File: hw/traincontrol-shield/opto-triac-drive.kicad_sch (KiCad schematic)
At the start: 6 parts, among them U5 MOC3021M, U6 MOC3021M

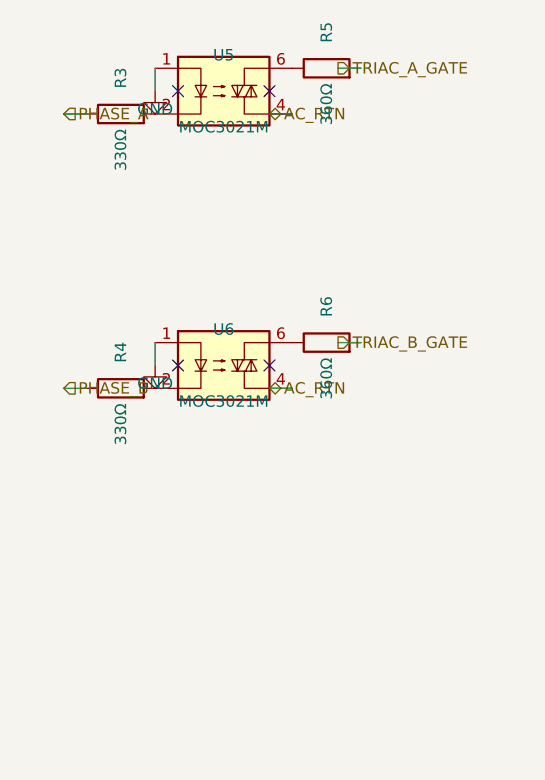
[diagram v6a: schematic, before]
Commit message: Disperse component layout and triple wire stub length across all sheets
- STUB: 2.54 → 7.62 mm (3×) in all three generator scripts
- Inter-component spacing doubled in power-supply, MCU, and logic sheets
- Top-level inter-column gap widened (LX 120 → 130 mm) to avoid label collision
- Sheet frame heights made variable per pin count (20–35 mm)
- Right-column sheet x-origin and connector J4/J5/J6 x-positions updated accordingly
- All 8 sheets regenerated and validated with kicad-cli

Co-Authored-By: Claude Sonnet 4.6 <noreply@anthropic.com>
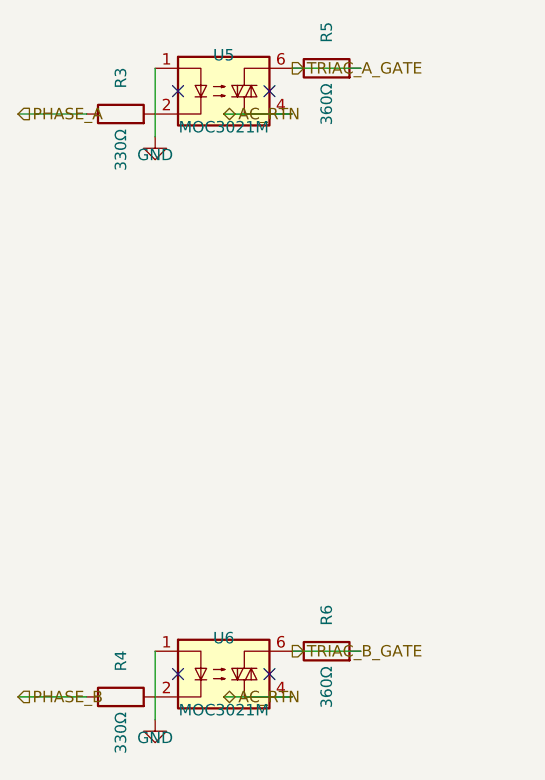
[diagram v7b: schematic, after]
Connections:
- net TRIAC_A_GATE: now also R5.1, U5.6
- net TRIAC_B_GATE: now also R6.1, U6.6
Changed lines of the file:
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@@
 	)
 	(wire
-		(pts (xy 72.39 87.63) (xy 72.39 90.17))
+		(pts (xy 72.39 87.63) (xy 72.39 95.25))
 		(stroke (width 0) (type solid))
 	)
 	(symbol
 		(lib_id "power:GND")
-		(at 72.39 90.17 0)
+		(at 72.39 95.25 0)
 		(unit 1)
 		(exclude_from_sim no)
@@
 		(dnp no)
 		(property "Reference" "#PWR03"
-			(at 72.39 88.17 0)
+			(at 72.39 93.25 0)
 			(effects (font (size 1.27 1.27)) (hide yes))
 		)
 		(property "Value" "GND"
-			(at 72.39 92.17 0)
+			(at 72.39 97.25 0)
 			(effects (font (size 1.27 1.27)))
 		)
 		(property "Footprint" ""
-			(at 72.39 90.17 0)
+			(at 72.39 95.25 0)
 			(effects (font (size 1.27 1.27)) (hide yes))
 		)
 		(property "Datasheet" ""
-			(at 72.39 90.17 0)
+			(at 72.39 95.25 0)
 			(effects (font (size 1.27 1.27)) (hide yes))
 		)
@@
 	)
 	(wire
-		(pts (xy 85.09 92.71000000000001) (xy 87.63000000000001 92.71000000000001))
+		(pts (xy 80.01 92.71000000000001) (xy 87.63000000000001 92.71000000000001))
 		(stroke (width 0) (type solid))
 	)
 	(hierarchical_label "AC_RTN"
 		(shape bidirectional)
-		(at 85.09 92.71000000000001 0)
-		(fields_autoplaced yes)
-		(effects (font (size 1.27 1.27)) (justify left bottom))
-		(property "Intersheetrefs" "${INTERSHEET_REFS}"
-			(at 85.09 92.71000000000001 0)
+		(at 80.01 92.71000000000001 0)
+		(fields_autoplaced yes)
+		(effects (font (size 1.27 1.27)) (justify left bottom))
+		(property "Intersheetrefs" "${INTERSHEET_REFS}"
+			(at 80.01 92.71000000000001 0)
 			(effects (font (size 1.27 1.27)) (hide yes))
 		)
@@
 	)
 	(wire
-		(pts (xy 62.23 92.71000000000001) (xy 64.77 92.71000000000001))
+		(pts (xy 57.15 92.71000000000001) (xy 64.77 92.71000000000001))
 		(stroke (width 0) (type solid))
 	)
 	(hierarchical_label "PHASE_A"
 		(shape input)
-		(at 62.23 92.71000000000001 0)
-		(fields_autoplaced yes)
-		(effects (font (size 1.27 1.27)) (justify left bottom))
-		(property "Intersheetrefs" "${INTERSHEET_REFS}"
-			(at 62.23 92.71000000000001 0)
+		(at 57.15 92.71000000000001 0)
+		(fields_autoplaced yes)
+		(effects (font (size 1.27 1.27)) (justify left bottom))
+		(property "Intersheetrefs" "${INTERSHEET_REFS}"
+			(at 57.15 92.71000000000001 0)
 			(effects (font (size 1.27 1.27)) (hide yes))
 		)
@@
 	)
 	(wire
-		(pts (xy 92.71000000000001 87.63) (xy 95.25000000000001 87.63))
+		(pts (xy 87.63000000000001 87.63) (xy 95.25000000000001 87.63))
 		(stroke (width 0) (type solid))
 	)
 	(hierarchical_label "TRIAC_A_GATE"
 		(shape output)
-		(at 92.71000000000001 87.63 0)
-		(fields_autoplaced yes)
-		(effects (font (size 1.27 1.27)) (justify left bottom))
-		(property "Intersheetrefs" "${INTERSHEET_REFS}"
-			(at 92.71000000000001 87.63 0)
+		(at 87.63000000000001 87.63 0)
+		(fields_autoplaced yes)
+		(effects (font (size 1.27 1.27)) (justify left bottom))
+		(property "Intersheetrefs" "${INTERSHEET_REFS}"
+			(at 87.63000000000001 87.63 0)
 			(effects (font (size 1.27 1.27)) (hide yes))
 		)
@@
 	(symbol
 		(lib_id "Relay_SolidState:MOC3021M")
-		(at 80.01 120.65 0)
+		(at 80.01 154.94 0)
 		(unit 1)
 		(exclude_from_sim no)
@@
 		(dnp no)
 		(property "Reference" "U6"
-			(at 80.01 116.65 0)
+			(at 80.01 150.94 0)
 			(effects (font (size 1.27 1.27)))
 		)
 		(property "Value" "MOC3021M"
-			(at 80.01 124.65 0)
+			(at 80.01 158.94 0)
 			(effects (font (size 1.27 1.27)))
 		)
 		(property "Footprint" "Package_DIP:DIP-6_W7.62mm"
-			(at 80.01 120.65 0)
-			(effects (font (size 1.27 1.27)) (hide yes))
-		)
-		(property "Datasheet" "~"
-			(at 80.01 120.65 0)
+			(at 80.01 154.94 0)
+			(effects (font (size 1.27 1.27)) (hide yes))
+		)
+		(property "Datasheet" "~"
+			(at 80.01 154.94 0)
 			(effects (font (size 1.27 1.27)) (hide yes))
 		)
@@
 	)
 	(wire
-		(pts (xy 72.39 118.11) (xy 72.39 120.65))
+		(pts (xy 72.39 152.4) (xy 72.39 160.02))
 		(stroke (width 0) (type solid))
 	)
 	(symbol
 		(lib_id "power:GND")
-		(at 72.39 120.65 0)
+		(at 72.39 160.02 0)
 		(unit 1)
 		(exclude_from_sim no)
@@
 		(dnp no)
 		(property "Reference" "#PWR04"
-			(at 72.39 118.65 0)
+			(at 72.39 158.02 0)
 			(effects (font (size 1.27 1.27)) (hide yes))
 		)
 		(property "Value" "GND"
-			(at 72.39 122.65 0)
+			(at 72.39 162.02 0)
 			(effects (font (size 1.27 1.27)))
 		)
 		(property "Footprint" ""
-			(at 72.39 120.65 0)
+			(at 72.39 160.02 0)
 			(effects (font (size 1.27 1.27)) (hide yes))
 		)
 		(property "Datasheet" ""
-			(at 72.39 120.65 0)
+			(at 72.39 160.02 0)
 			(effects (font (size 1.27 1.27)) (hide yes))
 		)
@@
 	)
 	(wire
-		(pts (xy 85.09 123.19000000000001) (xy 87.63000000000001 123.19000000000001))
+		(pts (xy 80.01 157.48) (xy 87.63000000000001 157.48))
 		(stroke (width 0) (type solid))
 	)
 	(hierarchical_label "AC_RTN"
 		(shape bidirectional)
-		(at 85.09 123.19000000000001 0)
-		(fields_autoplaced yes)
-		(effects (font (size 1.27 1.27)) (justify left bottom))
-		(property "Intersheetrefs" "${INTERSHEET_REFS}"
-			(at 85.09 123.19000000000001 0)
+		(at 80.01 157.48 0)
+		(fields_autoplaced yes)
+		(effects (font (size 1.27 1.27)) (justify left bottom))
+		(property "Intersheetrefs" "${INTERSHEET_REFS}"
+			(at 80.01 157.48 0)
 			(effects (font (size 1.27 1.27)) (hide yes))
 		)
@@
 	(symbol
 		(lib_id "Device:R")
-		(at 68.58 123.19000000000001 90)
+		(at 68.58 157.48 90)
 		(unit 1)
 		(exclude_from_sim no)
@@
 		(dnp no)
 		(property "Reference" "R4"
-			(at 68.58 119.19000000000001 0)
+			(at 68.58 153.48 0)
 			(effects (font (size 1.27 1.27)))
 		)
 		(property "Value" "330Ω"
-			(at 68.58 127.19000000000001 0)
+			(at 68.58 161.48 0)
 			(effects (font (size 1.27 1.27)))
 		)
 		(property "Footprint" "Resistor_SMD:R_0603_1608Metric"
-			(at 68.58 123.19000000000001 0)
-			(effects (font (size 1.27 1.27)) (hide yes))
-		)
-		(property "Datasheet" "~"
-			(at 68.58 123.19000000000001 0)
+			(at 68.58 157.48 0)
+			(effects (font (size 1.27 1.27)) (hide yes))
+		)
+		(property "Datasheet" "~"
+			(at 68.58 157.48 0)
 			(effects (font (size 1.27 1.27)) (hide yes))
 		)
@@
 	)
 	(wire
-		(pts (xy 62.23 123.19000000000001) (xy 64.77 123.19000000000001))
+		(pts (xy 57.15 157.48) (xy 64.77 157.48))
 		(stroke (width 0) (type solid))
 	)
 	(hierarchical_label "PHASE_B"
 		(shape input)
-		(at 62.23 123.19000000000001 0)
-		(fields_autoplaced yes)
-		(effects (font (size 1.27 1.27)) (justify left bottom))
-		(property "Intersheetrefs" "${INTERSHEET_REFS}"
-			(at 62.23 123.19000000000001 0)
+		(at 57.15 157.48 0)
+		(fields_autoplaced yes)
+		(effects (font (size 1.27 1.27)) (justify left bottom))
+		(property "Intersheetrefs" "${INTERSHEET_REFS}"
+			(at 57.15 157.48 0)
 			(effects (font (size 1.27 1.27)) (hide yes))
 		)
@@
 	(symbol
 		(lib_id "Device:R")
-		(at 91.44000000000001 118.11 90)
+		(at 91.44000000000001 152.4 90)
 		(unit 1)
 		(exclude_from_sim no)
@@
 		(dnp no)
 		(property "Reference" "R6"
-			(at 91.44000000000001 114.11 0)
+			(at 91.44000000000001 148.4 0)
 			(effects (font (size 1.27 1.27)))
 		)
 		(property "Value" "360Ω"
-			(at 91.44000000000001 122.11 0)
+			(at 91.44000000000001 156.4 0)
 			(effects (font (size 1.27 1.27)))
 		)
 		(property "Footprint" "Resistor_SMD:R_0603_1608Metric"
-			(at 91.44000000000001 118.11 0)
-			(effects (font (size 1.27 1.27)) (hide yes))
-		)
-		(property "Datasheet" "~"
-			(at 91.44000000000001 118.11 0)
+			(at 91.44000000000001 152.4 0)
+			(effects (font (size 1.27 1.27)) (hide yes))
+		)
+		(property "Datasheet" "~"
+			(at 91.44000000000001 152.4 0)
 			(effects (font (size 1.27 1.27)) (hide yes))
 		)
@@
 	)
 	(wire
-		(pts (xy 87.63000000000001 118.11) (xy 87.63000000000001 118.11))
-		(stroke (width 0) (type solid))
-	)
-	(wire
-		(pts (xy 92.71000000000001 118.11) (xy 95.25000000000001 118.11))
+		(pts (xy 87.63000000000001 152.4) (xy 87.63000000000001 152.4))
+		(stroke (width 0) (type solid))
+	)
+	(wire
+		(pts (xy 87.63000000000001 152.4) (xy 95.25000000000001 152.4))
 		(stroke (width 0) (type solid))
 	)
 	(hierarchical_label "TRIAC_B_GATE"
 		(shape output)
-		(at 92.71000000000001 118.11 0)
-		(fields_autoplaced yes)
-		(effects (font (size 1.27 1.27)) (justify left bottom))
-		(property "Intersheetrefs" "${INTERSHEET_REFS}"
-			(at 92.71000000000001 118.11 0)
+		(at 87.63000000000001 152.4 0)
+		(fields_autoplaced yes)
+		(effects (font (size 1.27 1.27)) (justify left bottom))
+		(property "Intersheetrefs" "${INTERSHEET_REFS}"
+			(at 87.63000000000001 152.4 0)
 			(effects (font (size 1.27 1.27)) (hide yes))
 		)
 	)
 	(no_connect
-		(at 74.93 120.65)
+		(at 74.93 154.94)
 	)
 	(no_connect
-		(at 85.09 120.65)
+		(at 85.09 154.94)
 	)
 	(sheet_instances
